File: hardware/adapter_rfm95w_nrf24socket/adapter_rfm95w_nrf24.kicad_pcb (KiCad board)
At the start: 2 copper layers, 45 x 53 mm, 4 parts, among them J1 Conn_02x04_Odd_Even, J2 DIO0, J3 3V3, J4 Conn_01x07

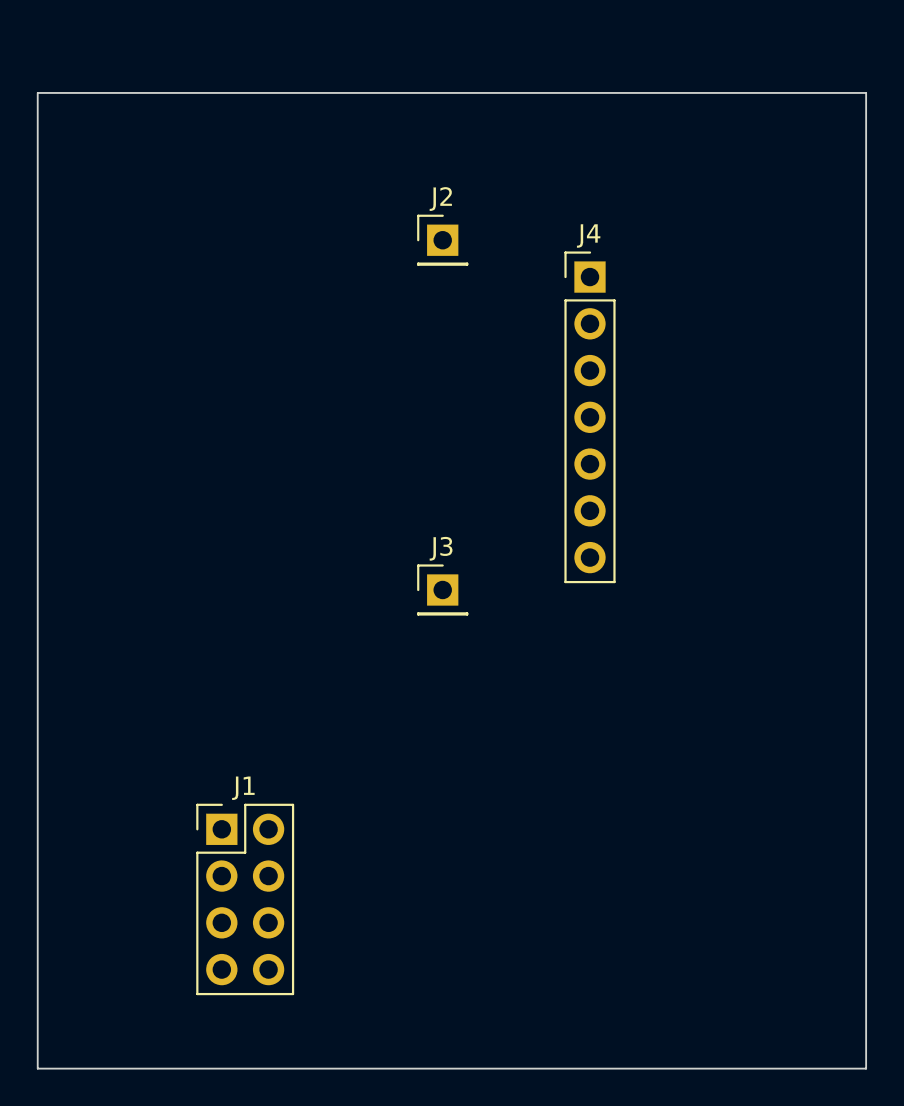
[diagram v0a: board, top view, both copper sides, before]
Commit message: feat: add KiCad design for RFM95W to NRF24 socket adapter
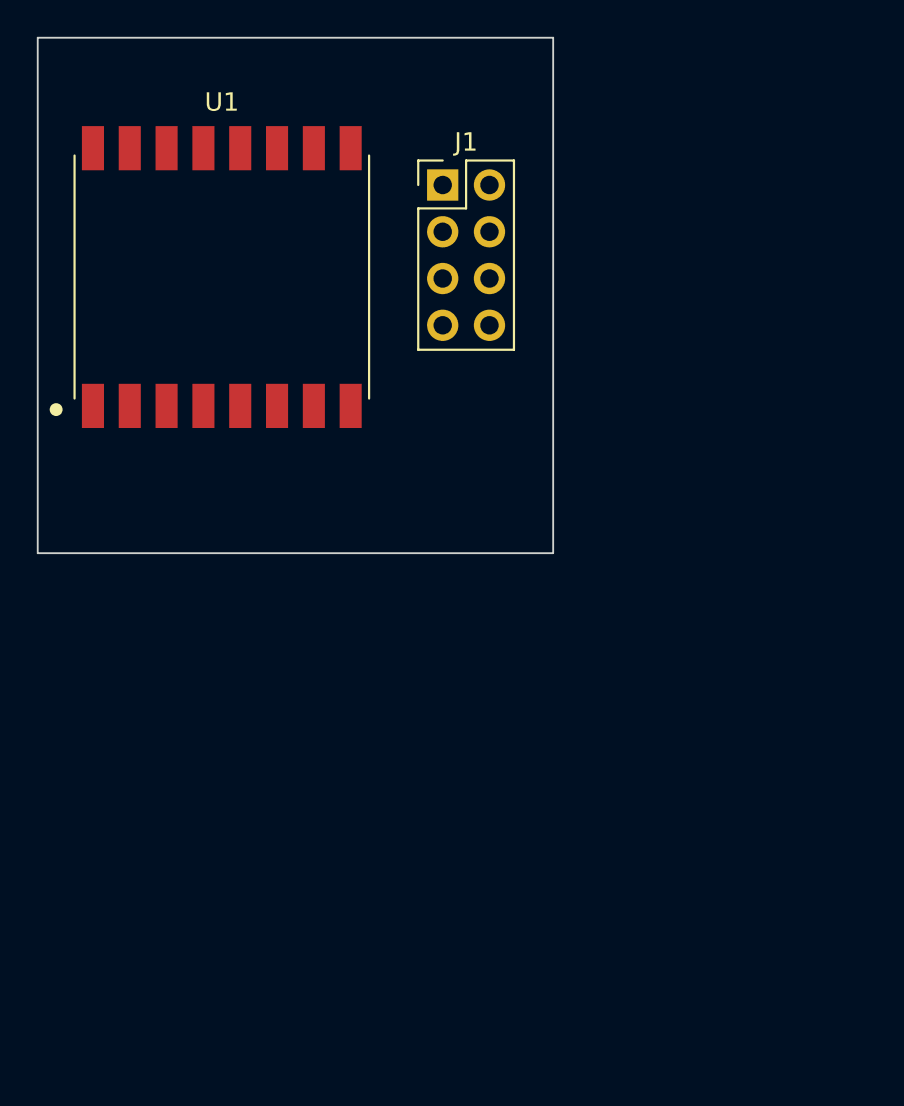
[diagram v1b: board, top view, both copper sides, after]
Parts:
- removed J2: DIO0, PinHeader_1x01_P2.54mm_Vertical
- removed J3: 3V3, PinHeader_1x01_P2.54mm_Vertical
- removed J4: Conn_01x07, PinHeader_1x07_P2.54mm_Vertical
- added U1: RFM95W_SMD_16P, M360_RFM95W:RFM95W_SMD_16P, F.Cu at (110.0, 105.0)
- moved J1 37.0 mm to (122.0, 100.0)
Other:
- board size 45 x 53 mm -> 28 x 28 mm
